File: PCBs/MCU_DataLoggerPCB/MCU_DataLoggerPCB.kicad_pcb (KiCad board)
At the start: 2 copper layers, 53.8 x 36.1 mm, 30 parts, among them J1 Conn_01x04_Pin, J2 Conn_01x04_Pin, J3 Conn_01x09_Pin, J4 Conn_02x03_Odd_Even, U1 24LC1025, U2 24LC1025, U3 DS1337S+, U4 ATMEGA328P-AU, Y1 32.768 kHz, Y2 16 MHz

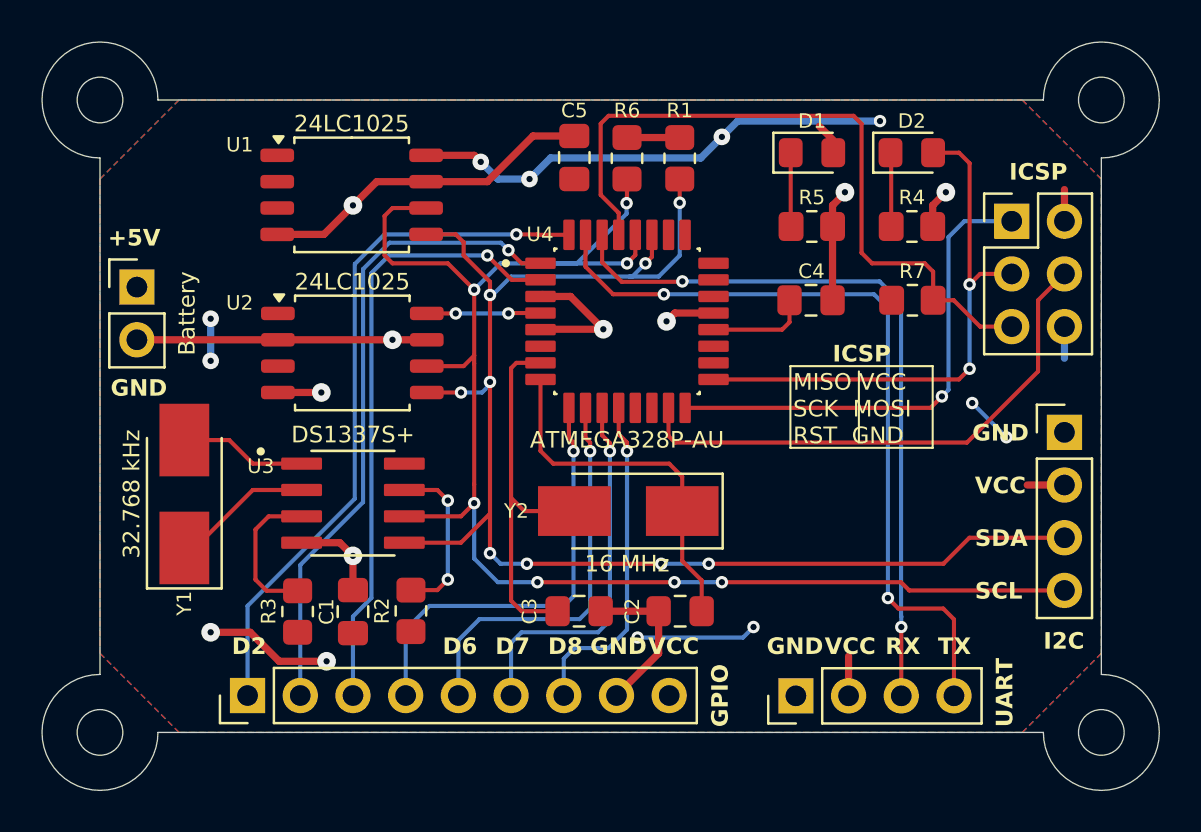
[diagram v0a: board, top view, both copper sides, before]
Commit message: Project: Completed 4-layer PCB routing
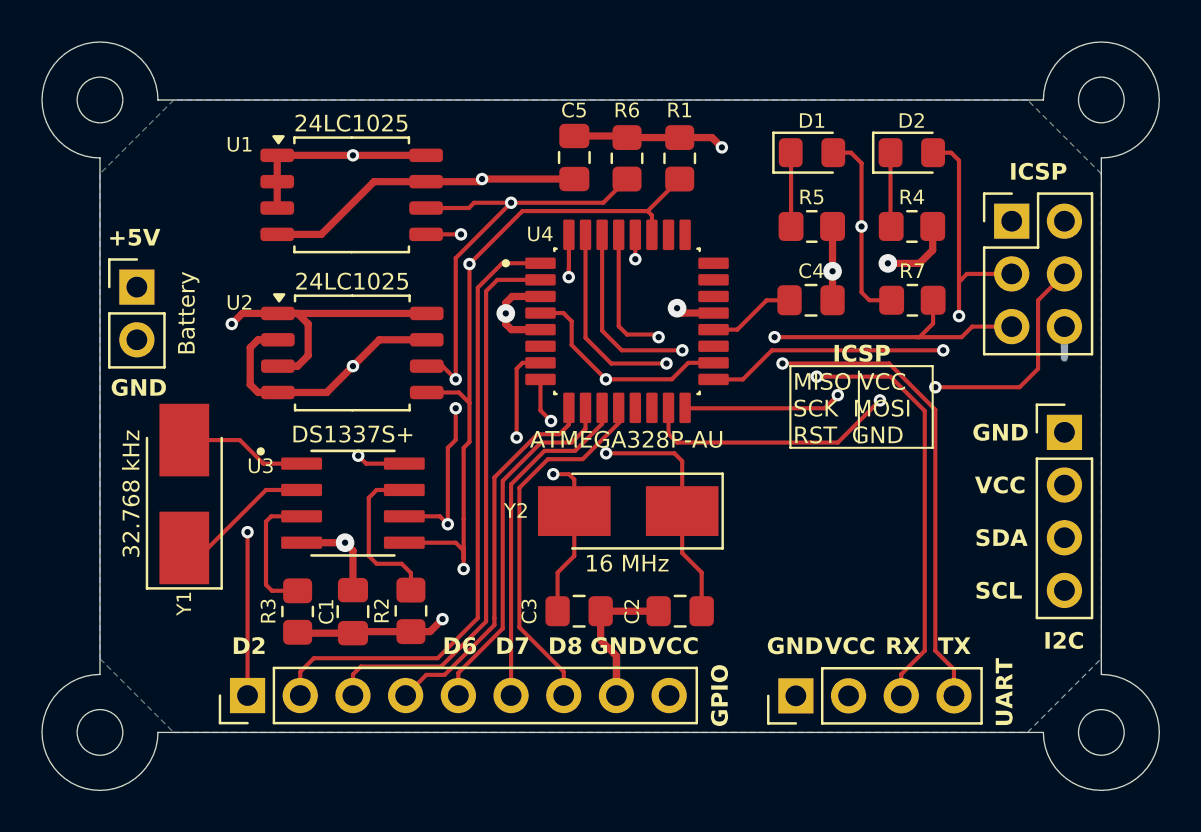
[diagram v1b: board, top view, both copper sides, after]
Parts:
- turned C5 to -90 degrees
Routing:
- net /VCC: track 48.5 -> 67.4 mm, vias 12 -> 7
- net /RESET: track 34.3 -> 26.0 mm, vias 0 -> 2
- net GND: track 69.0 -> 60.9 mm, vias 10 -> 7
- net /MISO: track 23.8 -> 19.5 mm
- net Net-(U4-PB6): track 18.5 -> 14.9 mm, vias 0 -> 2
- net /SDA: track 70.1 -> 67.1 mm, vias 9 -> 3
- net /D5: track 21.1 -> 18.3 mm, vias 1 -> 0
- net /D2: track 33.8 -> 36.6 mm, vias 1 -> 2
- net /D4: track 29.7 -> 27.3 mm, vias 1 -> 0
- net /D6: track 19.4 -> 17.3 mm, vias 1 -> 0
- net /D7: track 18.2 -> 16.5 mm, vias 1 -> 0
- net /SCK: track 26.7 -> 25.2 mm
- net /D8: track 16.3 -> 17.7 mm, vias 1 -> 0
- net /SCL: track 73.1 -> 72.0 mm, vias 7 -> 5
- net /D3: track 31.3 -> 30.2 mm, vias 1 -> 0
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- added copper zone on In2.Cu, net /VCC
- removed copper zone on F.Cu, net /VCC
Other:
- copper layers 2 -> 4
